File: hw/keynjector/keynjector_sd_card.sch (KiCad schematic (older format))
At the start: 5 parts, among them J4 492250821

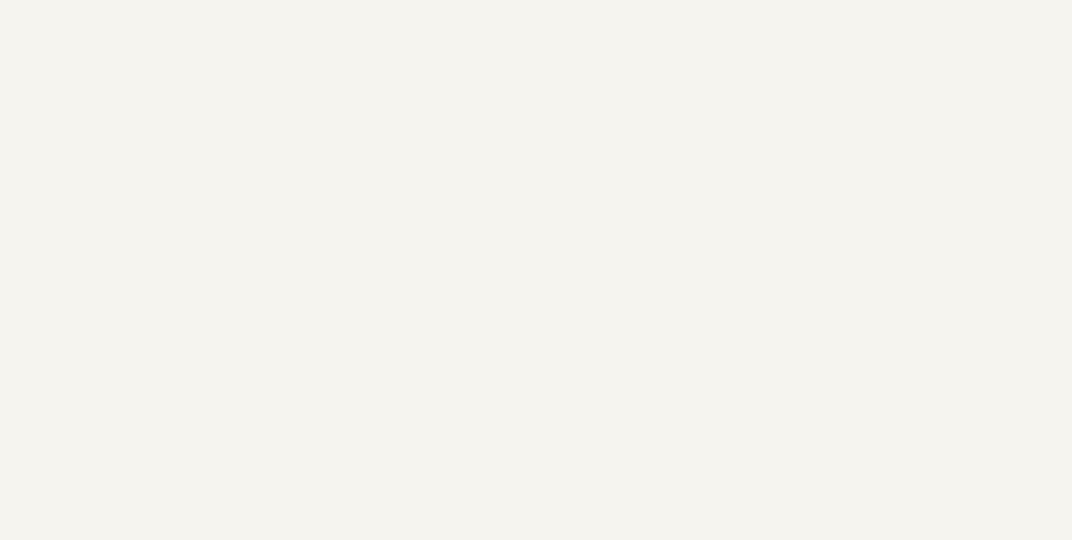
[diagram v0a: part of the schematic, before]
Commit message: added license text to KiCad sheets
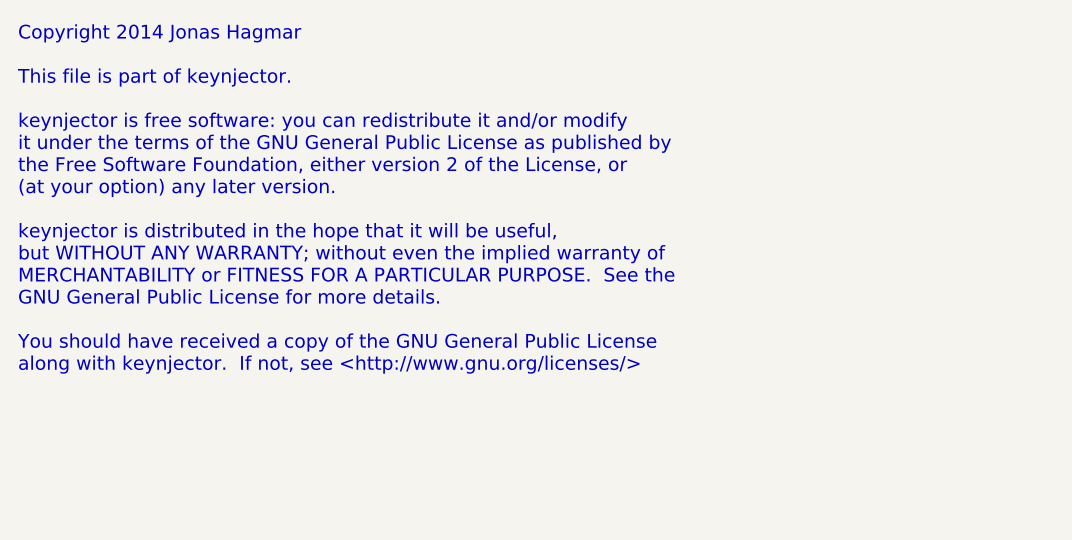
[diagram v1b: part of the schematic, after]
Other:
- note added: "Copyright 2014 Jonas Hagmar\n\nThis file is part of keynjector.\n\nkeynjector is free software: you can redistribute it and/or modify\nit under the terms of the GNU General Public License as published by\nthe Free Software Foundation, either version 2 of the License, or\n(at your option) any later version.\n\nkeynjector is distributed in the hope that it will be useful,\nbut WITHOUT ANY WARRANTY;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"
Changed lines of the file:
@@
 Sheet 7 7
 Title ""
-Date "6 nov 2014"
+Date "2 dec 2014"
 Rev ""
 Comp ""
@@
 Text Notes 6200 3200 0    60   ~ 0
 Pull up MCDA0-MCDA3 and C/D_A.
+Text Notes 850  800  0    60   ~ 0
+Copyright 2014 Jonas Hagmar\n\nThis file is part of keynjector.\n\nkeynjector is free software: you can redistribute it and/or modify\nit under the terms of the GNU General Public License as published by\nthe Free Software Foundation, either version 2 of the License, or\n(at your option) any later version.\n\nkeynjector is distributed in the hope that it will be useful,\nbut WITHOUT ANY WARRANTY; without even the implied warranty of\nMERCHANTABILITY or FITNESS FOR A PARTICULAR PURPOSE.  See the\nGNU General Public License for more details.\n\nYou should have received a copy of the GNU General Public License\nalong with keynjector.  If not, see <http://www.gnu.org/licenses/>
 $EndSCHEMATC
